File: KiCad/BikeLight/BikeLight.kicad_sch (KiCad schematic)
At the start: 15 parts, among them J1 Conn-01x02_P2.5mm_S2B-XH-A-BK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, J3 Conn-01x02_P2.5mm_S2B-XH-A-BK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, SW1 CK_KMS2xxG, U1 HT-CT62, U2 MPU-6050, U3 MCP1826S-33, U4 MAX17048, U5 TP4056-42-ESOP8, U6 MT3608

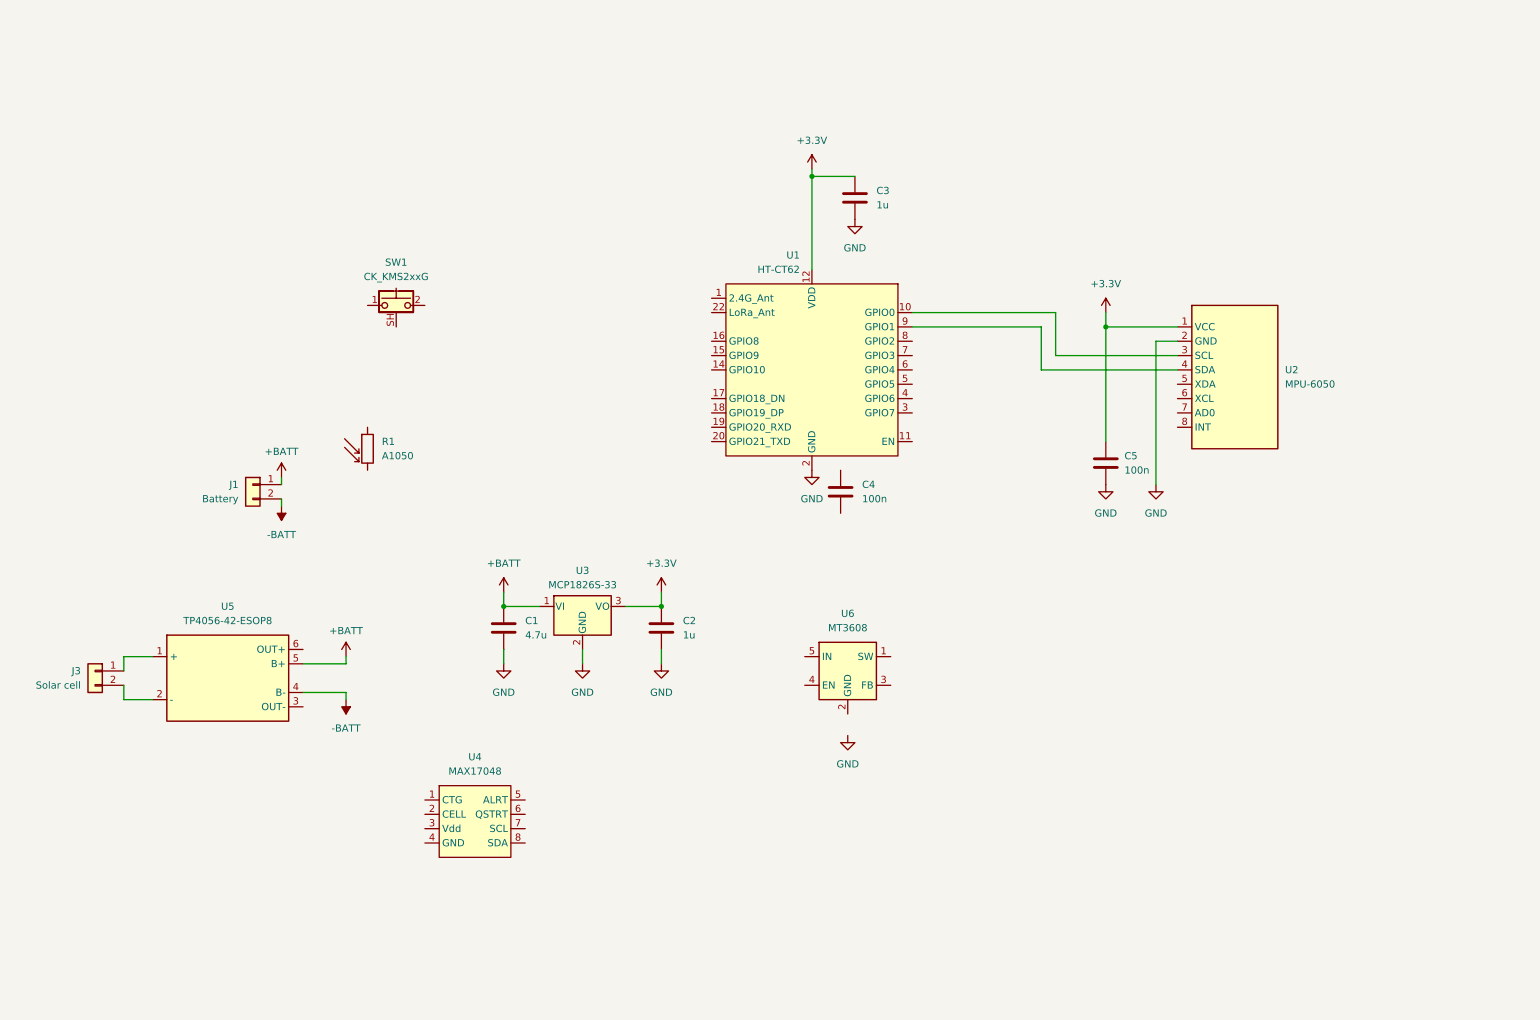
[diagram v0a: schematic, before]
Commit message: Updated schematic, added datasheet
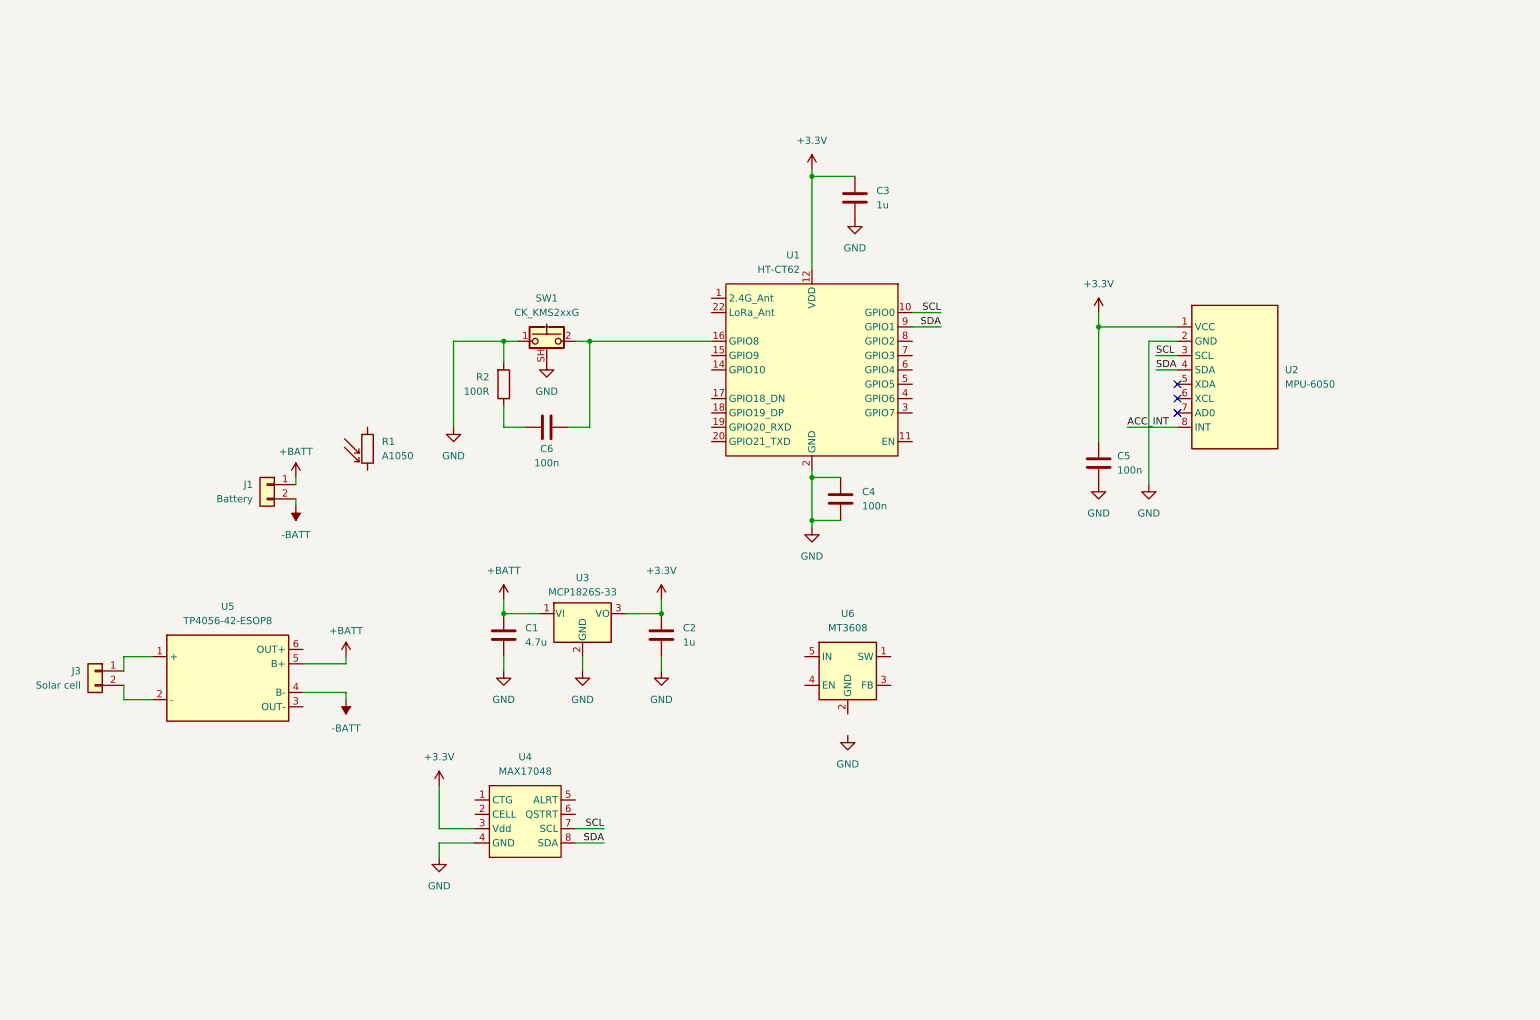
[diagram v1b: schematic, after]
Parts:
- added C6: 100n_0603_TCC0603X7R104K500CT, Capacitor_SMD:C_0603_1608Metric, symbol 00-kiml-capacitors-smd:100n_0603_TCC0603X7R104K500CT
- added R2: 100R_0603_RC0603FR-07100RL, Resistor_SMD:R_0603_1608Metric, symbol 00-kiml-resistors-smd:100R_0603_RC0603FR-07100RL
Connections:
- net +3.3V: now also U4.3 (Vdd)
- net GND: now also C4.1, C4.2, SW1.1, SW1.SH (B), U4.4 (GND), R2.2
- net SCL: now reaches U1.10 (GPIO0), U2.3 (SCL)
- net SCL: now also U4.7 (SCL)
- net SDA: now reaches U1.9 (GPIO1), U2.4 (SDA)
- net SDA: now also U4.8 (SDA)
- net ACC_INT: now reaches U2.8 (INT)
- net at U1.16 (GPIO8): now also SW1.2, C6.2
- new net: C6.1, R2.1
- no-connect marks 0 -> 3
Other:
- moved on the sheet: C1, C2, C4, C5, J1, SW1, U3, U4

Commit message: started with pcb
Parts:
- added C7: 100n_0603_TCC0603X7R104K500CT, Capacitor_SMD:C_0603_1608Metric, symbol 00-kiml-capacitors-smd:100n_0603_TCC0603X7R104K500CT
- U2: footprint Sensor_Motion:InvenSense_QFN-24_4x4mm_P0.5mm -> Personal_Library:GY-521_Angled
- U4: footprint (none) -> Personal_Library:SON50P200X200X80-9N
- U5: footprint Package_SO:SOIC-8-1EP_3.9x4.9mm_P1.27mm_EP2.41x3.3mm_ThermalVias -> Personal_Library:TP4056-18650
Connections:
- net +3.3V: no longer U4.3 (Vdd)
- net +BATT: now also U4.2 (CELL), U4.3 (Vdd), C7.1
- net -BATT: now also U4.4 (GND), C7.2
- net GND: now also U4.1 (CTG), U4.6 (QSTRT); no longer U4.4 (GND)
- net ~{ALRT}: now reaches U4.5 (~{ALRT})

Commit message: More Schematic
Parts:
- added U7: ~, symbol Personal_Library:RFID-RC522
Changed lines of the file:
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@@
 			"AJoGwQFNQyvQNPQ2gnQXIBAIBAKB/Jb0d78MAoFAIBBIjwPdBQgEAoFAIDyA7gIEAoFAIBAeQHcB"
 			"AoFAIBAID6C7AIFAIBAIhAfQXYBAIBAIBMID6C5AIBAIBALhAXQXIBAIBAKB8AC6CxAIBAKBQHgA"
-			"3QUIBAKBQCA8gO4CBAKBQCAQHkB3AQKBQCAQCA/+D1GXigLguG4WAAAAAElFTkSuQmCC"
+			"3QUIBAKBQCA8gO4CBAKBQCAQHkB3AQKBQCAQCA/+D1GXigLguG4WAAAAAElFTkSuQmCCAAAEAAAA"
+			"AAAAAEAvyfzUAQAAAAAAAAAAAACI8bib+38AAAIAAAAGAAAAkAHe/NQBAABgh9781AEAALiH3vzU"
+			"AQAA/////wAAAAAAAAAAAAAAAAAAAAAAAAAAAQAAAAAAAAD/AAAAAAAAAB8AAAAAAAAAAAAAAAAA"
+			"AAAAAAAAAAABAAAAAAAAAAAAAAAAAAAAAAAAAAAAAAAAAAAAAAAAAAAAAAAAAAAAAAAAAAAAAAAA"
+			"AAAAAAAAAAAAAAAAAAAAAAAAAAAAAAAAAAAAAAAAAAAAAAAAAAAAAAAAAAAAAAAAAAAAAAAAAAAA"
+			"AAAAAAAAAAAAAAAAAAAAAAAAAAAAAAAAAAAAAAAAAAAAAAAAAAAAAAAAAAAAAAAAAAAAAAAAAAAA"
+			"AAAAAAAAAAAAAAAAAAAAAAAAAAAAAAAAAAAAAAAAAAAAAAAAAAAAAAAAAAAAAAAAAAAAAAAAAAAA"
+			"AAAAAAAAAAAAAAAAAAAAAAAAAAAAAAAAAAAAAAAAAAAAAAAAAAAAAAAAAAAAAPAAAAAAAAAALuh0"
+			"7QAJAIBwAd781AEAAACa3vzUAQAAEJre/NQBAAAAEAAAAAAAAIjxuJv7fwAAAgAAAAYAAABYi978"
+			"1AEAAKgQ3vzUAQAAABHe/NQBAAAPAAAAAAAAAAAAAAAAAAAAAAAAAAAAAAABAAAABAAAAP8AAAAA"
+			"AAAAAwAAAAAAAAAAAAAAAAAAAAAAAAAAAAEAYPG4m/t/AAABAAAABgAAAFiL3vzUAQAAAAve/NQB"
+			"AABYC9781AEAAA8AAAAAAAAAAAAAAAAAAAAAAAAAAAAAAAEAAAAEAAAA/wAAAAAAAAADAAAAAAAA"
+			"AAAAAAAAAAAABAAAAAAAAADgrqr81AEAAAAAAAAAAAAAsPG4m/t/AAADAAAAEQAAAAAAAAAAAAAA"
+			"aA3e/NQBAADADd781AEAAAEAAAAAAAAAAAAAAAAAAAAAAAAAAAAAAAEAAAAAAAAA/wAAAAAAAAAA"
+			"AAAAAAAAANoEAd+4pPsJoL7M/NQBAACAAvr71AEAAAIAAAAAAAAAeIre/NQBAABoD6v81AEAAFCL"
+			"3vzUAQAAAAAAAAAAAAAAAAAAAACAPxi+x/zUAQAAAAAAAAAAAAAAARAAAAAAAAAAAAAAAAAAAAAA"
+			"AAAAAADw5If81AEAAODkh/zUAQAAsEHO/NQBAAAAAAAAAAAAAPDkh/zUAQAA4OSH/NQBAADQQc78"
+			"1AEAAAAAAAAAAAAAIAAAAG0CAAAAAAAAAAAAACgcAAAAAAAAAAABAAAAAABA98n81AEAAKoCAAAA"
+			"AAAAIK2q/NQBAAD/////AAD//wAAAAABAAAAAAAAAAAAAAAAAAAAAAAAAAAAAAAAAA=="
 		)
 	)
@@
 					(unit 1)
 				)
+			)
+		)
+	)
+	(symbol
+		(lib_id "Personal_Library:RFID-RC522")
+		(at 185.42 118.11 0)
+		(unit 1)
+		(exclude_from_sim no)
+		(in_bom yes)
+		(on_board yes)
+		(dnp no)
+		(property "Reference" "U7"
+			(at 185.674 119.38 0)
+			(effects
+				(font
+					(size 1.27 1.27)
+				)
+				(justify left)
+			)
+		)
+		(property "Value" "~"
+			(at 201.93 133.35 0)
+			(effects
+				(font
+					(size 1.27 1.27)
+				)
+				(justify left)
+			)
+		)
+		(property "Footprint" ""
+			(at 185.42 118.11 0)
+			(effects
+				(font
+					(size 1.27 1.27)
+				)
+				(hide yes)
+			)
+		)
+		(property "Datasheet" ""
+			(at 185.42 118.11 0)
+			(effects
+				(font
+					(size 1.27 1.27)
+				)
+				(hide yes)
+			)
+		)
+		(property "Description" ""
+			(at 185.42 118.11 0)
+			(effects
+				(font
+					(size 1.27 1.27)
+				)
+				(hide yes)
+			)
+		)
+		(pin "2"
+		)
+		(pin "6"
+		)
+		(pin "3"
+		)
+		(pin "8"
+		)
+		(pin "5"
+		)
+		(pin "4"
+		)
+		(pin "1"
+		)
+		(pin "7"
+		)
+		(instances
+			(project ""
+				(path "/bc4a3ac7-23ef-4452-9888-c2aa5f8e2382"
+					(reference "U7")
+					(unit 1)
+				)
